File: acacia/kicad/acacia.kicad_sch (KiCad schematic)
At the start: 127 parts, among them J1 USB4500-03-0-A, SW1 A, SW10 C, SW11 R, SW12 F, SW13 V, SW14 T, SW15 G, SW16 Back, SW17 Gui, SW18 Ctl, SW19 Alt, SW2 Z, SW20 Sft, SW21 Fwd, SW22 AltGr, SW23 L1, SW24 L2, SW25 Ctl, SW26 U, SW27 J, SW28 M, SW29 H, SW3 Esc, SW30 N, SW31 I, SW32 K, SW33 Comm, SW34 O, SW35 L, SW36 Dot, SW38 P, SW39 Semi, SW4 B, SW40 Slsh, SW41 Y, SW42 Png, SW43 QMK, SW48 Q, SW49 RESET, SW5 W, SW6 S, SW7 X, SW8 E, SW9 D, U1 USBLC6-2SC6, U2 ATmega32U2-A, Y1 16MHz

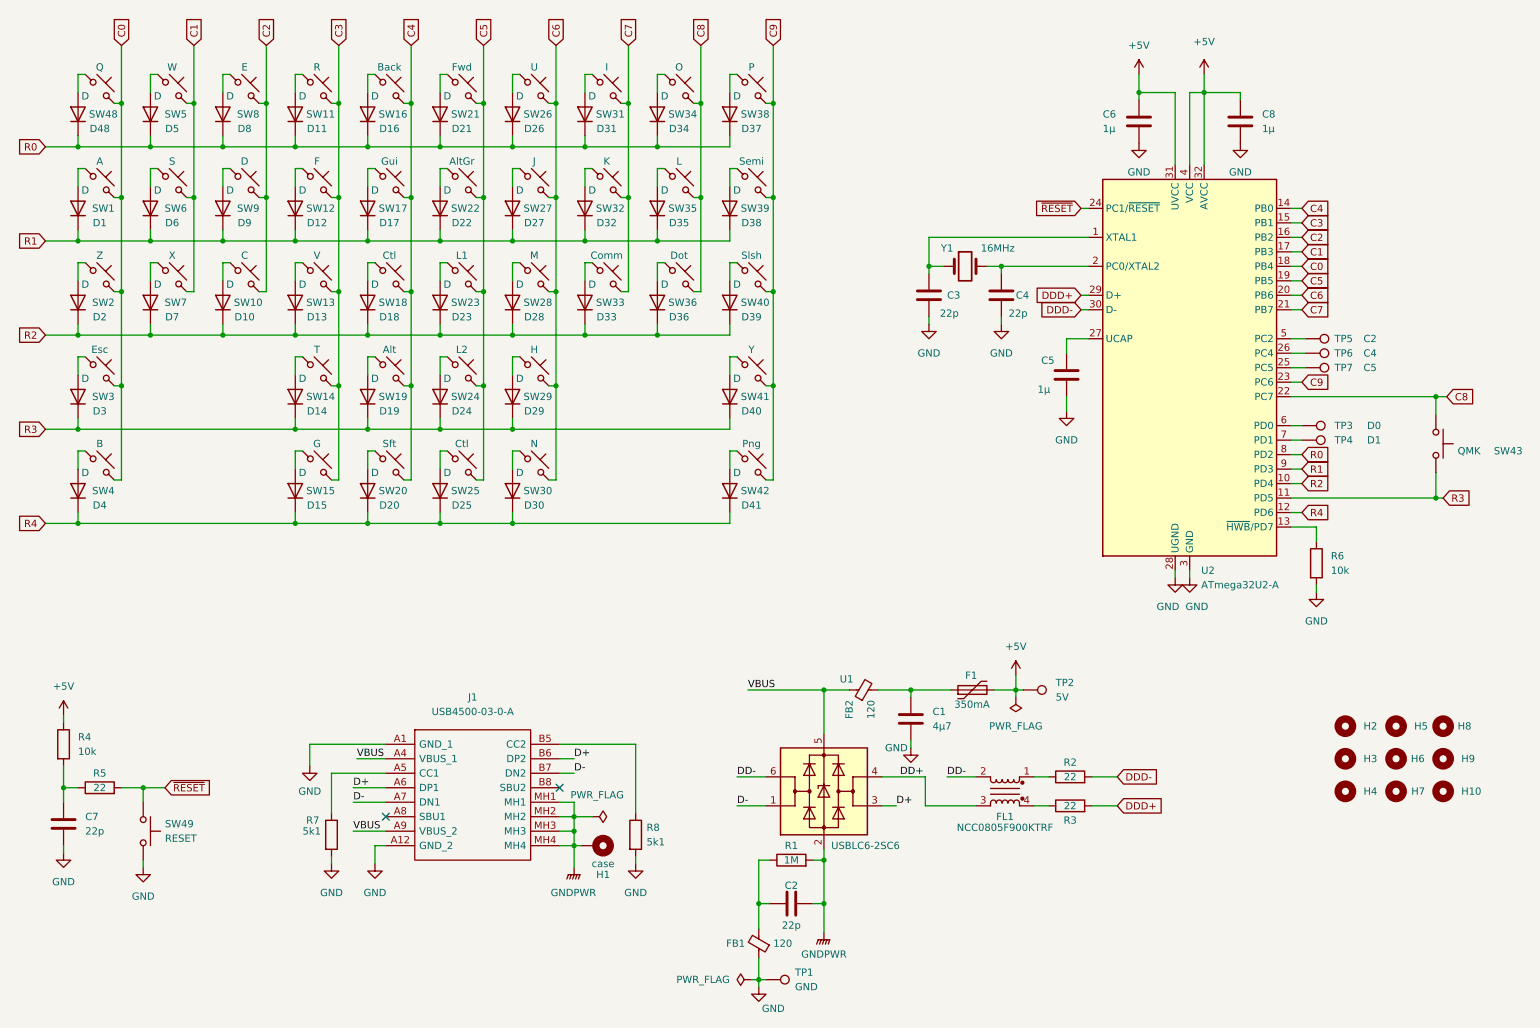
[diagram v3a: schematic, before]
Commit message: keys routed
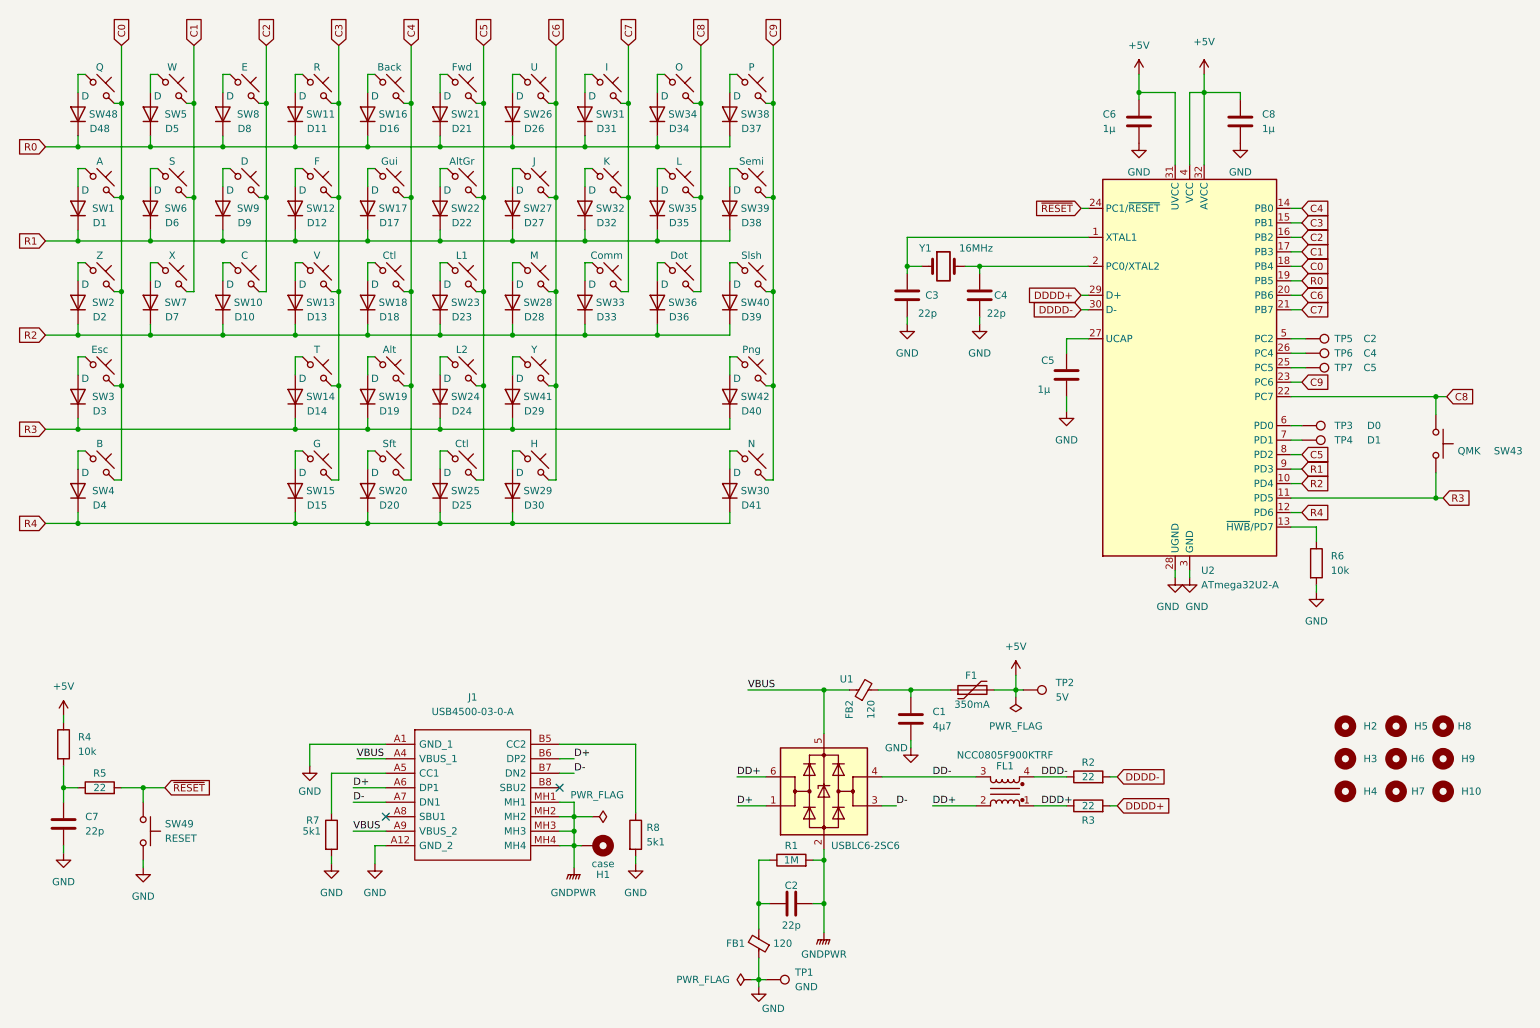
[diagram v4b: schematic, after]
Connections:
- net C5: now also U2.8 (PD2); no longer U2.19 (PB5)
- net C6: now also SW41.2; no longer SW30.2
- net C9: now also SW30.2; no longer SW41.2
- net D+: now also U1.1 (I/O1); no longer U1.3 (I/O2)
- net D-: now also U1.3 (I/O2); no longer U1.1 (I/O1)
- net DD+: now also FL1.2, U1.6 (I/O1); no longer FL1.3, U1.4 (I/O2)
- net DD-: now also FL1.3, U1.4 (I/O2); no longer FL1.2, U1.6 (I/O1)
- net DDD+: now also FL1.1, R3.1; no longer R3.2, U2.29 (D+)
- net DDD-: now also FL1.4, R2.1; no longer R2.2, U2.30 (D-)
- net R0: now also U2.19 (PB5); no longer U2.8 (PD2)
- net at SW30.1: now also D41.2 (A); no longer D30.2 (A)
- net at SW29.1: now also D30.2 (A); no longer D29.2 (A)
- net at SW42.1: now also D40.2 (A); no longer D41.2 (A)
- net at SW41.1: now also D29.2 (A); no longer D40.2 (A)
- new net DDDD+: R3.2, U2.29 (D+)
- new net DDDD-: R2.2, U2.30 (D-)
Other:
- moved on the sheet: C3, C4, FL1, R2, R3, SW29, SW30, SW41, SW42, Y1

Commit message: routing
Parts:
- removed H1: case, MountingHole:MountingHole_3.2mm_M3_ISO14580_Pad, symbol Mechanical:MountingHole_Pad
- added H1: MountingHole, MountingHole:MountingHole_3.2mm_M3, symbol Mechanical:MountingHole
- SW23: value L1 -> L2
- SW24: value L2 -> L1
- SW29: value H -> N
- SW3: value Esc -> Tab
- SW30: value N -> Enter
- SW41: value Y -> H
- SW42: value Png -> Y
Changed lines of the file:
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@@
-    (stroke (width 0) (type default) (color 0 0 0 0))
-  )
-  (wire (pts (xy 114.3 160.655) (xy 115.57 160.655))
     (stroke (width 0) (type default) (color 0 0 0 0))
   )
@@
     (in_bom yes) (on_board yes)
     (property "Reference" "SW30" (id 0) (at 146.05 98.425 0))
-    (property "Value" "N" (id 1) (at 145.415 90.17 0))
+    (property "Value" "Enter" (id 1) (at 145.415 90.17 0))
     (property "Footprint" "mech-kbd:MX-Hotswap-1U" (id 2) (at 145.415 93.98 0)
       (effects (font (size 1.27 1.27)) hide)
@@
     (pin "2")
   )
+  (symbol (lib_id "Mechanical:MountingHole") (at 249.555 133.985 0) (unit 1)
+    (in_bom yes) (on_board yes) (fields_autoplaced)
+    (property "Reference" "H1" (id 0) (at 252.73 133.9849 0)
+      (effects (font (size 1.27 1.27)) (justify left))
+    )
+    (property "Value" "MountingHole" (id 1) (at 252.095 135.2549 0)
+      (effects (font (size 1.27 1.27)) (justify left) hide)
+    )
+    (property "Footprint" "MountingHole:MountingHole_3.2mm_M3" (id 2) (at 249.555 133.985 0)
+      (effects (font (size 1.27 1.27)) hide)
+    )
+    (property "Datasheet" "~" (id 3) (at 249.555 133.985 0)
+      (effects (font (size 1.27 1.27)) hide)
+    )
+  )
   (symbol (lib_id "Switch:SW_Push_45deg") (at 69.215 77.47 0) (unit 1)
     (in_bom yes) (on_board yes)
@@
     (in_bom yes) (on_board yes)
     (property "Reference" "SW24" (id 0) (at 95.25 81.915 0))
-    (property "Value" "L2" (id 1) (at 94.615 73.66 0))
+    (property "Value" "L1" (id 1) (at 94.615 73.66 0))
     (property "Footprint" "mech-kbd:MX-Hotswap-1.25U" (id 2) (at 94.615 77.47 0)
       (effects (font (size 1.27 1.27)) hide)
@@
     (in_bom yes) (on_board yes)
     (property "Reference" "SW29" (id 0) (at 107.95 98.425 0))
-    (property "Value" "H" (id 1) (at 107.315 90.17 0))
+    (property "Value" "N" (id 1) (at 107.315 90.17 0))
     (property "Footprint" "mech-kbd:MX-Hotswap-1U" (id 2) (at 107.315 93.98 0)
       (effects (font (size 1.27 1.27)) hide)
@@
     (in_bom yes) (on_board yes)
     (property "Reference" "SW23" (id 0) (at 95.25 65.405 0))
-    (property "Value" "L1" (id 1) (at 94.615 57.15 0))
+    (property "Value" "L2" (id 1) (at 94.615 57.15 0))
     (property "Footprint" "mech-kbd:MX-Hotswap-1.5U" (id 2) (at 94.615 60.96 0)
       (effects (font (size 1.27 1.27)) hide)
@@
     (in_bom yes) (on_board yes)
     (property "Reference" "SW42" (id 0) (at 146.05 81.915 0))
-    (property "Value" "Png" (id 1) (at 145.415 73.66 0))
+    (property "Value" "Y" (id 1) (at 145.415 73.66 0))
     (property "Footprint" "mech-kbd:MX-Hotswap-1U" (id 2) (at 145.415 77.47 0)
       (effects (font (size 1.27 1.27)) hide)
@@
     (pin "1")
     (pin "2")
-  )
-  (symbol (lib_id "Mechanical:MountingHole_Pad") (at 118.11 160.655 270) (unit 1)
-    (in_bom yes) (on_board yes)
-    (property "Reference" "H1" (id 0) (at 119.38 165.735 90))
-    (property "Value" "case" (id 1) (at 119.38 163.83 90))
-    (property "Footprint" "MountingHole:MountingHole_3.2mm_M3_ISO14580_Pad" (id 2) (at 118.11 160.655 0)
-      (effects (font (size 1.27 1.27)) hide)
-    )
-    (property "Datasheet" "~" (id 3) (at 118.11 160.655 0)
-      (effects (font (size 1.27 1.27)) hide)
-    )
-    (pin "1")
   )
   (symbol (lib_id "Device:D") (at 78.105 32.385 90) (unit 1)
@@
     (in_bom yes) (on_board yes)
     (property "Reference" "SW3" (id 0) (at 31.75 81.915 0))
-    (property "Value" "Esc" (id 1) (at 31.115 73.66 0))
+    (property "Value" "Tab" (id 1) (at 31.115 73.66 0))
     (property "Footprint" "mech-kbd:MX-Hotswap-1U" (id 2) (at 31.115 77.47 0)
       (effects (font (size 1.27 1.27)) hide)
@@
     (in_bom yes) (on_board yes)
     (property "Reference" "SW41" (id 0) (at 107.95 81.915 0))
-    (property "Value" "Y" (id 1) (at 107.315 73.66 0))
+    (property "Value" "H" (id 1) (at 107.315 73.66 0))
     (property "Footprint" "mech-kbd:MX-Hotswap-1U" (id 2) (at 107.315 77.47 0)
       (effects (font (size 1.27 1.27)) hide)
@@
       (reference "FL1") (unit 1) (value "NCC0805F900KTRF") (footprint "Inductor_SMD:L_CommonModeChoke_Coilcraft_0805USB")
     )
-    (path "/9d4ce2ac-7235-4453-b413-199c3973ecfb"
-      (reference "H1") (unit 1) (value "case") (footprint "MountingHole:MountingHole_3.2mm_M3_ISO14580_Pad")
+    (path "/6bc121fe-2438-4af1-8315-9841407df752"
+      (reference "H1") (unit 1) (value "MountingHole") (footprint "MountingHole:MountingHole_3.2mm_M3")
     )
     (path "/dfc9ecc8-fcc9-40db-bacc-8477d0798b91"
@@
     )
     (path "/be6a0cfb-4c75-41e3-b913-e6230c72c9ba"
-      (reference "SW3") (unit 1) (value "Esc") (footprint "mech-kbd:MX-Hotswap-1U")
+      (reference "SW3") (unit 1) (value "Tab") (footprint "mech-kbd:MX-Hotswap-1U")
     )
     (path "/35374ce0-5407-4c4c-98cd-131c157d8ee4"
@@
     )
     (path "/8570441d-16f0-4cad-80d1-abdb8e08df85"
-      (reference "SW23") (unit 1) (value "L1") (footprint "mech-kbd:MX-Hotswap-1.5U")
+      (reference "SW23") (unit 1) (value "L2") (footprint "mech-kbd:MX-Hotswap-1.5U")
     )
     (path "/6fc8cc91-cbf7-4a3d-ac0e-9701fbff1bc8"
-      (reference "SW24") (unit 1) (value "L2") (footprint "mech-kbd:MX-Hotswap-1.25U")
+      (reference "SW24") (unit 1) (value "L1") (footprint "mech-kbd:MX-Hotswap-1.25U")
     )
     (path "/0f491137-ae10-4a69-973d-b9ebebd6fb93"
@@
     )
     (path "/700eb7e6-d32b-4476-b67d-0a1353726bb8"
-      (reference "SW29") (unit 1) (value "H") (footprint "mech-kbd:MX-Hotswap-1U")
+      (reference "SW29") (unit 1) (value "N") (footprint "mech-kbd:MX-Hotswap-1U")
     )
     (path "/044e1c8b-d3e4-48bf-96ce-94ecd1c7165e"
-      (reference "SW30") (unit 1) (value "N") (footprint "mech-kbd:MX-Hotswap-1U")
+      (reference "SW30") (unit 1) (value "Enter") (footprint "mech-kbd:MX-Hotswap-1U")
     )
     (path "/bfa4e7ee-9929-4880-8506-ea362fbf8c1b"
@@
     )
     (path "/c059c3e6-cfe2-482d-9a8f-f8d8d51f01c4"
-      (reference "SW41") (unit 1) (value "Y") (footprint "mech-kbd:MX-Hotswap-1U")
+      (reference "SW41") (unit 1) (value "H") (footprint "mech-kbd:MX-Hotswap-1U")
     )
     (path "/86f47fed-4e68-451e-8f68-09f9af160924"
-      (reference "SW42") (unit 1) (value "Png") (footprint "mech-kbd:MX-Hotswap-1U")
+      (reference "SW42") (unit 1) (value "Y") (footprint "mech-kbd:MX-Hotswap-1U")
     )
     (path "/e1cf7695-ef7b-492c-a736-c3a29ef34af9"
